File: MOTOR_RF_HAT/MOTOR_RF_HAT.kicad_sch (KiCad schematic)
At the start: 26 parts, among them J4 Conn_01x01, J5 Conn_01x01, Q1 BSS138, U4 XT30PW-M, U5 LMR51420YFDDCR

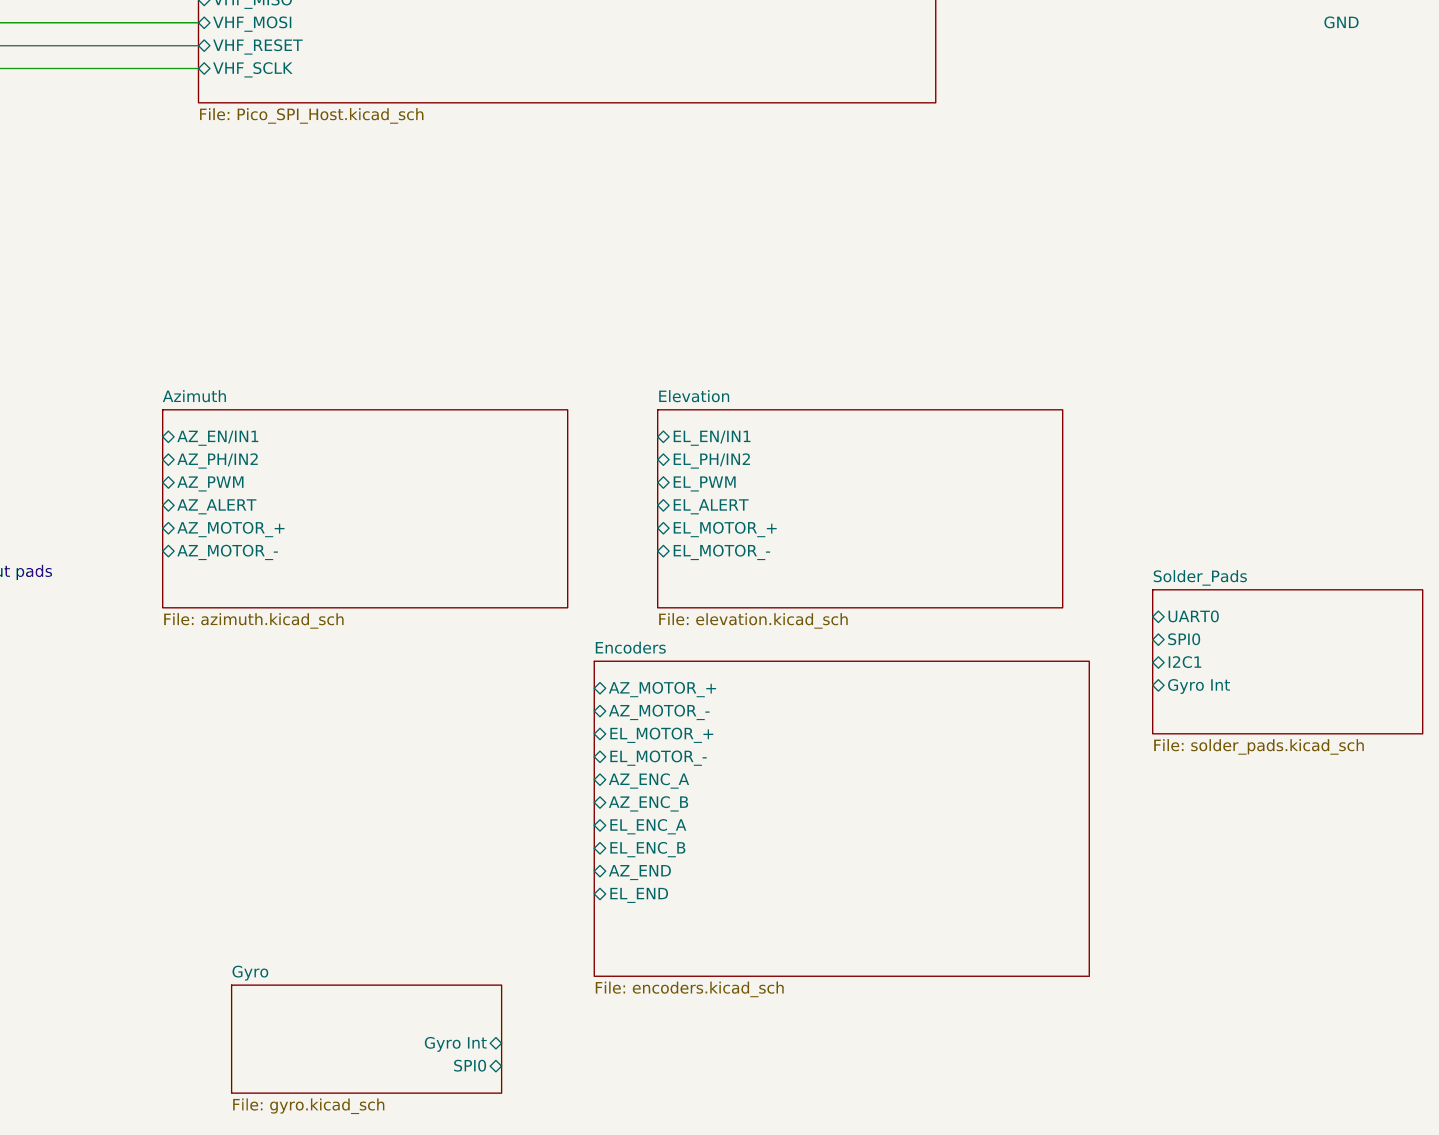
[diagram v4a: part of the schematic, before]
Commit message: MOTOR_RF_HAT: fix TestPoint:smallpad → components:smallpad in solder_pads
All 18 test point footprint references in solder_pads.kicad_sch now
point to the local components:smallpad instead of TestPoint:smallpad
(which doesn't exist in KiCad's global TestPoint library).

Co-Authored-By: Claude Opus 4.6 (1M context) <noreply@anthropic.com>
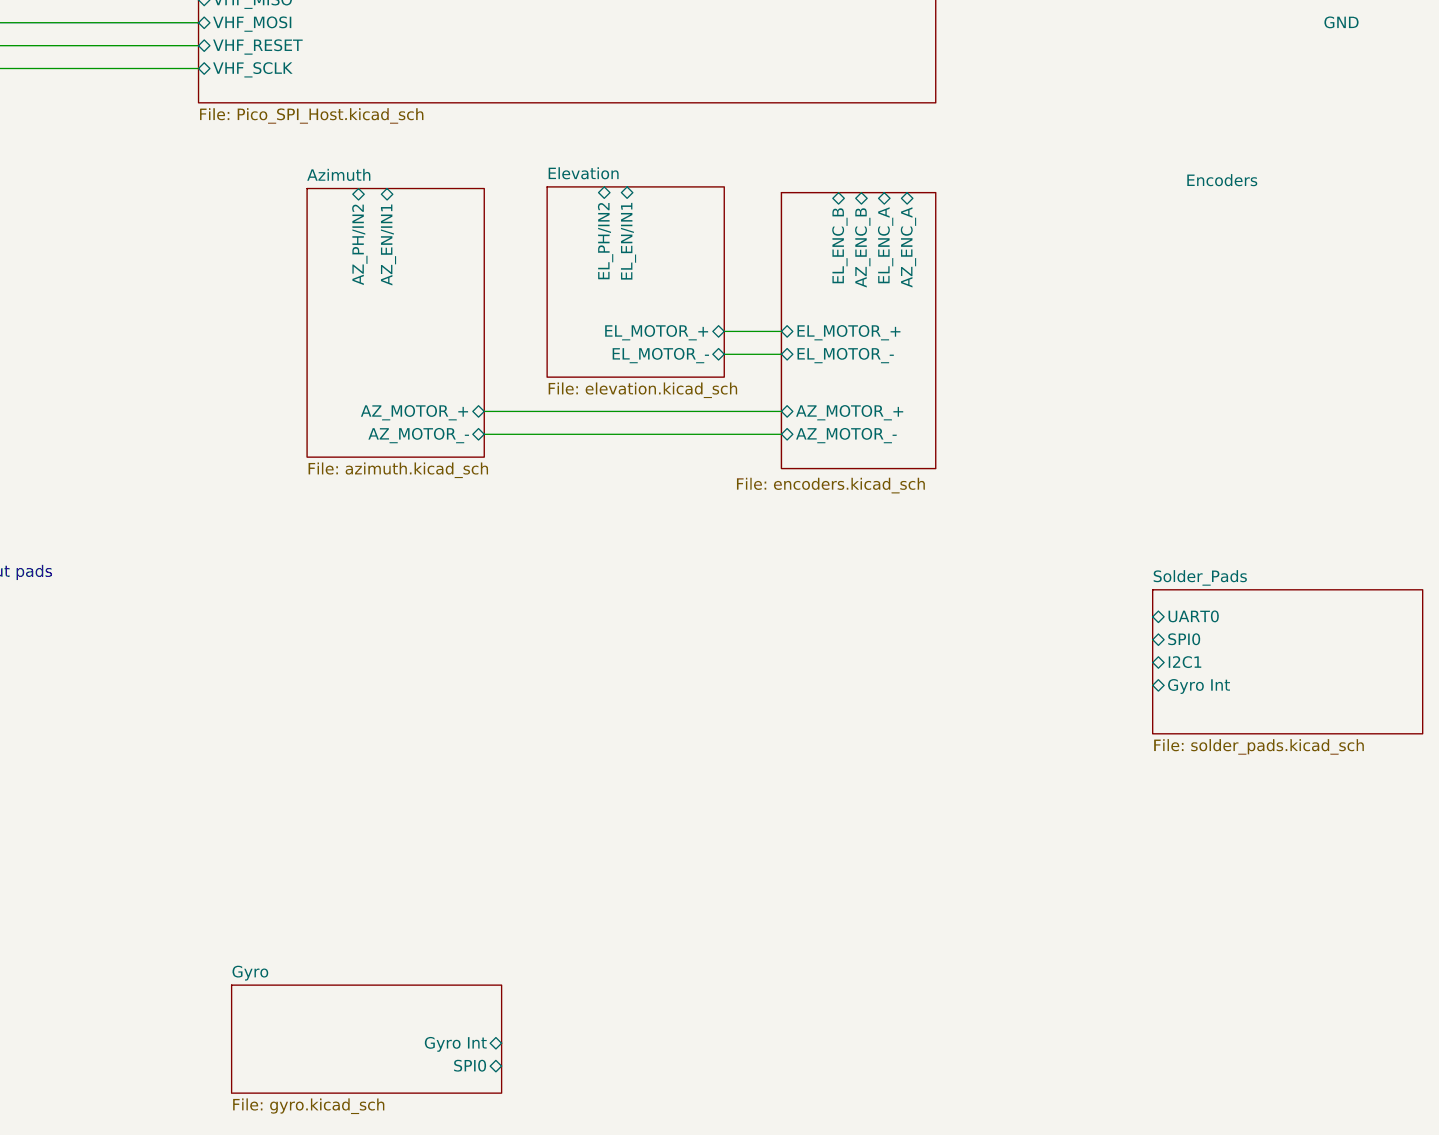
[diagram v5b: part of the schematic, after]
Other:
- sheet Azimuth ports: added none; removed AZ_ALERT, AZ_PWM
- sheet Elevation ports: added none; removed EL_ALERT, EL_PWM
- sheet Encoders ports: added none; removed AZ_END, EL_END
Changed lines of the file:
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@@
 		)
 	)
+	(wire
+		(pts
+			(xy 125.73 170.18) (xy 158.75 170.18)
+		)
+		(stroke
+			(width 0)
+			(type default)
+		)
+	)
 	(bus
 		(pts
@@
 	(wire
 		(pts
+			(xy 152.4 163.83) (xy 158.75 163.83)
+		)
+		(stroke
+			(width 0)
+			(type default)
+		)
+	)
+	(wire
+		(pts
 			(xy 68.58 121.92) (xy 93.98 121.92)
 		)
@@
 	(wire
 		(pts
+			(xy 152.4 161.29) (xy 158.75 161.29)
+		)
+		(stroke
+			(width 0)
+			(type default)
+		)
+	)
+	(wire
+		(pts
 			(xy 81.28 34.29) (xy 81.28 36.83)
 		)
@@
 	(wire
 		(pts
+			(xy 125.73 172.72) (xy 158.75 172.72)
+		)
+		(stroke
+			(width 0)
+			(type default)
+		)
+	)
+	(wire
+		(pts
 			(xy 44.45 29.21) (xy 59.69 29.21)
 		)
@@
 			)
 		)
-		(property "Footprint" "components:smallpad"
+		(property "Footprint" ""
 			(at 64.77 175.26 0)
 			(hide yes)
@@
 	)
 	(sheet
-		(at 145 170)
-		(size 45 22)
+		(at 132.715 145.235)
+		(size 19.685 21.135)
 		(exclude_from_sim no)
 		(in_bom yes)
@@
 		)
 		(property "Sheetname" "Elevation"
-			(at 145 169.2884 0)
+			(at 132.715 144.5234 0)
 			(show_name no)
 			(do_not_autoplace no)
@@
 		)
 		(property "Sheetfile" "elevation.kicad_sch"
-			(at 145 192.5846 0)
+			(at 132.715 166.9546 0)
 			(show_name no)
 			(do_not_autoplace no)
@@
 		)
 		(pin "EL_EN{slash}IN1" bidirectional
-			(at 145 173 180)
+			(at 141.605 145.235 90)
 			(effects
 				(font
 					(size 1.27 1.27)
 				)
-				(justify left)
+				(justify right)
 			)
 		)
 		(pin "EL_PH{slash}IN2" bidirectional
-			(at 145 175.54 180)
+			(at 139.065 145.235 90)
 			(effects
 				(font
 					(size 1.27 1.27)
 				)
-				(justify left)
-			)
-		)
-		(pin "EL_PWM" bidirectional
-			(at 145 178.08 180)
-			(effects
-				(font
-					(size 1.27 1.27)
-				)
-				(justify left)
-			)
-		)
-		(pin "EL_ALERT" bidirectional
-			(at 145 180.62 180)
-			(effects
-				(font
-					(size 1.27 1.27)
-				)
-				(justify left)
+				(justify right)
 			)
 		)
 		(pin "EL_MOTOR_+" bidirectional
-			(at 145 183.16 180)
+			(at 152.4 161.29 0)
 			(effects
 				(font
 					(size 1.27 1.27)
 				)
-				(justify left)
+				(justify right)
 			)
 		)
 		(pin "EL_MOTOR_-" bidirectional
-			(at 145 185.7 180)
+			(at 152.4 163.83 0)
 			(effects
 				(font
 					(size 1.27 1.27)
 				)
-				(justify left)
+				(justify right)
 			)
 		)
@@
 	)
 	(sheet
-		(at 90 170)
-		(size 45 22)
+		(at 106.045 145.415)
+		(size 19.685 29.845)
 		(exclude_from_sim no)
 		(in_bom yes)
@@
 		)
 		(property "Sheetname" "Azimuth"
-			(at 90 169.2884 0)
+			(at 106.045 144.7034 0)
 			(show_name no)
 			(do_not_autoplace no)
@@
 		)
 		(property "Sheetfile" "azimuth.kicad_sch"
-			(at 90 192.5846 0)
+			(at 106.045 175.8446 0)
 			(show_name no)
 			(do_not_autoplace no)
@@
 		)
 		(pin "AZ_EN{slash}IN1" bidirectional
-			(at 90 173 180)
+			(at 114.935 145.415 90)
 			(effects
 				(font
 					(size 1.27 1.27)
 				)
-				(justify left)
+				(justify right)
 			)
 		)
 		(pin "AZ_PH{slash}IN2" bidirectional
-			(at 90 175.54 180)
+			(at 111.76 145.415 90)
 			(effects
 				(font
 					(size 1.27 1.27)
 				)
-				(justify left)
-			)
-		)
-		(pin "AZ_PWM" bidirectional
-			(at 90 178.08 180)
-			(effects
-				(font
-					(size 1.27 1.27)
-				)
-				(justify left)
-			)
-		)
-		(pin "AZ_ALERT" bidirectional
-			(at 90 180.62 180)
-			(effects
-				(font
-					(size 1.27 1.27)
-				)
-				(justify left)
+				(justify right)
 			)
 		)
 		(pin "AZ_MOTOR_+" bidirectional
-			(at 90 183.16 180)
+			(at 125.73 170.18 0)
 			(effects
 				(font
 					(size 1.27 1.27)
 				)
-				(justify left)
+				(justify right)
 			)
 		)
 		(pin "AZ_MOTOR_-" bidirectional
-			(at 90 185.7 180)
+			(at 125.73 172.72 0)
 			(effects
 				(font
 					(size 1.27 1.27)
 				)
-				(justify left)
+				(justify right)
 			)
 		)
@@
 	)
 	(sheet
-		(at 137.955 197.94)
-		(size 55 35)
+		(at 158.75 145.87)
+		(size 17.145 30.66)
 		(exclude_from_sim no)
 		(in_bom yes)
 		(on_board yes)
 		(dnp no)
-		(fields_autoplaced yes)
 		(stroke
 			(width 0.1524)
@@
 		)
 		(property "Sheetname" "Encoders"
-			(at 137.955 197.2284 0)
+			(at 203.675 145.288 0)
 			(show_name no)
 			(do_not_autoplace no)
@@
 		)
 		(property "Sheetfile" "encoders.kicad_sch"
-			(at 137.955 233.5246 0)
+			(at 153.637 177.546 0)
 			(show_name no)
 			(do_not_autoplace no)
@@
 		)
 		(pin "AZ_MOTOR_+" bidirectional
-			(at 137.955 200.94 180)
+			(at 158.75 170.18 180)
 			(effects
 				(font
@@
 		)
 		(pin "AZ_MOTOR_-" bidirectional
-			(at 137.955 203.48 180)
+			(at 158.75 172.72 180)
 			(effects
 				(font
@@
 		)
 		(pin "EL_MOTOR_+" bidirectional
-			(at 137.955 206.02 180)
+			(at 158.75 161.29 180)
 			(effects
 				(font
@@
 		)
 		(pin "EL_MOTOR_-" bidirectional
-			(at 137.955 208.56 180)
+			(at 158.75 163.83 180)
 			(effects
 				(font
@@
 		)
 		(pin "AZ_ENC_A" bidirectional
-			(at 137.955 211.1 180)
+			(at 172.72 145.87 90)
 			(effects
 				(font
 					(size 1.27 1.27)
 				)
-				(justify left)
+				(justify right)
 			)
 		)
 		(pin "AZ_ENC_B" bidirectional
-			(at 137.955 213.64 180)
+			(at 167.64 145.87 90)
 			(effects
 				(font
 					(size 1.27 1.27)
 				)
-				(justify left)
+				(justify right)
 			)
 		)
 		(pin "EL_ENC_A" bidirectional
-			(at 137.955 216.18 180)
+			(at 170.18 145.87 90)
 			(effects
 				(font
 					(size 1.27 1.27)
 				)
-				(justify left)
+				(justify right)
 			)
 		)
 		(pin "EL_ENC_B" bidirectional
-			(at 137.955 218.72 180)
+			(at 165.1 145.87 90)
 			(effects
 				(font
 					(size 1.27 1.27)
 				)
-				(justify left)
-			)
-		)
-		(pin "AZ_END" bidirectional
-			(at 137.955 221.26 180)
-			(effects
-				(font
-					(size 1.27 1.27)
-				)
-				(justify left)
-			)
-		)
-		(pin "EL_END" bidirectional
-			(at 137.955 223.8 180)
-			(effects
-				(font
-					(size 1.27 1.27)
-				)
-				(justify left)
+				(justify right)
 			)
 		)

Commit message: MOTOR_RF_HAT: add TestPoint lib alias to fix persistent smallpad errors
KiCad's lib_symbols cache keeps reverting footprint refs to
TestPoint:smallpad on save. Added TestPoint as a footprint library
alias pointing to components.pretty so both TestPoint:smallpad and
components:smallpad resolve to the same local footprint.

Co-Authored-By: Claude Opus 4.6 (1M context) <noreply@anthropic.com>
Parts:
- renumbered C19 to C1, C22 to C2, C24 to C3, C48 to C4, C49 to C5, C50 to C6, C51 to C7, D3 to D2, D2 to D3, H4 to H2, H5 to H3, H6 to H4, J4 to J1, J5 to J2, L18 to L1, R16 to R1, R17 to R2, TP19 to TP1, U4 to U1, U5 to U2

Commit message: MOTOR_RF_HAT: 0805→0603 passives, encoder caps 100nF→100pF
- Changed all capacitor and resistor footprints from 0805 to 0603
  across all schematic sheets (CC1200 UHF/VHF, root, azimuth,
  elevation, encoders)
- Fixed encoder RC filter caps C68-C71 from 100nF to 100pF
  (fc = 15.9 MHz, transparent to 35 kHz encoder signal)

Co-Authored-By: Claude Opus 4.6 (1M context) <noreply@anthropic.com>
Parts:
- added TP2: MOSI, components:smallpad, symbol Connector:TestPoint_Small
- added TP3: CLK, components:smallpad, symbol Connector:TestPoint_Small
- added TP4: CS, components:smallpad, symbol Connector:TestPoint_Small
- added TP5: 3.3V, components:smallpad, symbol Connector:TestPoint_Small
- added TP6: GND, components:smallpad, symbol Connector:TestPoint_Small
- C1: footprint Capacitor_SMD:C_0805_2012Metric -> Capacitor_SMD:C_0603_1608Metric
- TP1: value TestPoint_Small -> MISO
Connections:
- net +3V3: now also TP5.1
- net CC1200_VHF_144MHz/VHF_MISO: now also TP1.1
- net CC1200_VHF_144MHz/VHF_MOSI: now also TP2.1
- net CC1200_VHF_144MHz/VHF_SCLK: now also TP3.1
- net GND: now also TP6.1
- new net Pico_SPI_Host/IMU_CS: TP4.1
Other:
- removed sheet Gyro
- removed sheet Solder_Pads
- sheet CC1200_UHF_432MHz ports: added none; removed UHF_GPIO2, UHF_GPIO3
- sheet CC1200_VHF_144MHz ports: added none; removed VHF_GPIO0, VHF_GPIO2, VHF_GPIO3
- sheet Pico_SPI_Host ports: added AZ_ENC_A, AZ_ENC_B, AZ_IN1, AZ_IN2, EL_ENC_A, EL_ENC_B, EL_IN1, EL_IN2, IMU_CS; removed UHF_GPIO2, UHF_GPIO3, VHF_GPIO0, VHF_GPIO2, VHF_GPIO3
- note added: "IMU Signals"
- note removed: "add breakout pads"
- moved on the sheet: TP1

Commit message: MOTOR_RF_HAT: fix cap packages — 10uF/50V, 22uF, 4.7uF/50V back to 0805
These values cannot physically fit in 0603:
- C1 (4.7uF 50V): 0603→0805
- C3 (22uF): 0603→0805
- C60-C62 (10uF AZ motor VBB bypass): 0603→0805
- C64-C66 (10uF EL motor VBB bypass): 0603→0805

All other passives remain 0603.

Co-Authored-By: Claude Opus 4.6 (1M context) <noreply@anthropic.com>
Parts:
- C1, C3: footprint Capacitor_SMD:C_0603_1608Metric -> Capacitor_SMD:C_0805_2012Metric
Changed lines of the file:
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@@
 			)
 		)
-		(property "Footprint" "Capacitor_SMD:C_0603_1608Metric"
+		(property "Footprint" "Capacitor_SMD:C_0805_2012Metric"
 			(at 133.0452 45.72 0)
 			(hide yes)
@@
 			)
 		)
-		(property "Footprint" "Capacitor_SMD:C_0603_1608Metric"
+		(property "Footprint" "Capacitor_SMD:C_0805_2012Metric"
 			(at 45.4152 45.72 0)
 			(hide yes)
